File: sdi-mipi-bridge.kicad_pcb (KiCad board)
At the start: 6 copper layers, 70 x 42 mm, 203 parts, among them J1 112740-13, J2 112740-13, J3 WE_68715014522_ONE-SIDE, J4 GRPB052VWVN-RC, J5 GRPB041VWVN-RC, J6 GRPB052VWVN-RC, SW1 SW_DIP_x06, SW2 SW_DIP_x06, U1 MAX8902B, U2 GS2971A, U3 GS2988, U4 CrossLink_LIF-MD6000-6JMG80I, U5 SC18IS602BIPW, Y1 ABM7_27.000MH_D2Y_T

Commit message: Change RST pullup from 2k2 to 4k7 and note I2C pull-ups as DNP
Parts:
- R84: value R_2k2_0402 -> R_4k7_0402

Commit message: Bump release to 1.3.0
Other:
- board text added: "Rev.1.3.0 02/2021"
- board text removed: "Rev.1.2.0 12/2020"
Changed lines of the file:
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@@
-(kicad_pcb (version 20171130) (host pcbnew "(5.1.8-0-10_14)")
+(kicad_pcb (version 20171130) (host pcbnew 5.1.5+dfsg1-2~bpo10+1)
   (general
     (thickness 1.6)
@@
     (37 F.SilkS user)
     (38 B.Mask user)
-    (39 F.Mask user hide)
+    (39 F.Mask user)
     (40 Dwgs.User user hide)
     (41 Cmts.User user hide)
@@
   (gr_line (start 154.14 124.39) (end 152 122.25) (layer B.SilkS) (width 0.1))
   (gr_line (start 156.08 124.39) (end 154.14 124.39) (layer B.SilkS) (width 0.1))
-  (gr_text "Rev.1.2.0 12/2020" (at 145.5234 103.6068) (layer F.Mask)
+  (gr_text "Rev.1.3.0 02/2021" (at 145.5234 103.6068) (layer F.Mask)
     (effects (font (size 0.7 0.7) (thickness 0.15)))
   )
@@
     (effects (font (size 1 1) (thickness 0.2)))
   )
-  (gr_text "Rev.1.2.0 12/2020" (at 145.5234 103.6068) (layer F.Cu)
+  (gr_text "Rev.1.3.0 02/2021" (at 145.5234 103.6068) (layer F.Cu)
     (effects (font (size 0.7 0.7) (thickness 0.15)))
   )

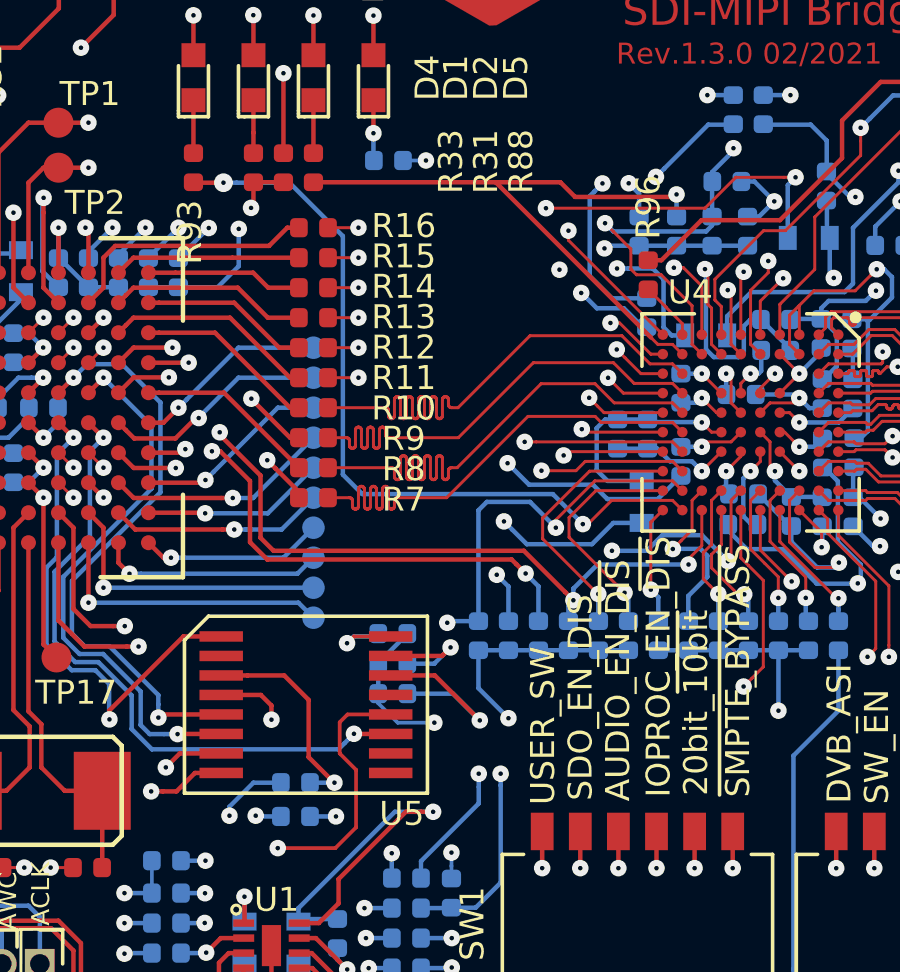
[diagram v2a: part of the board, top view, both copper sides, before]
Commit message: Update layout DRC-clean
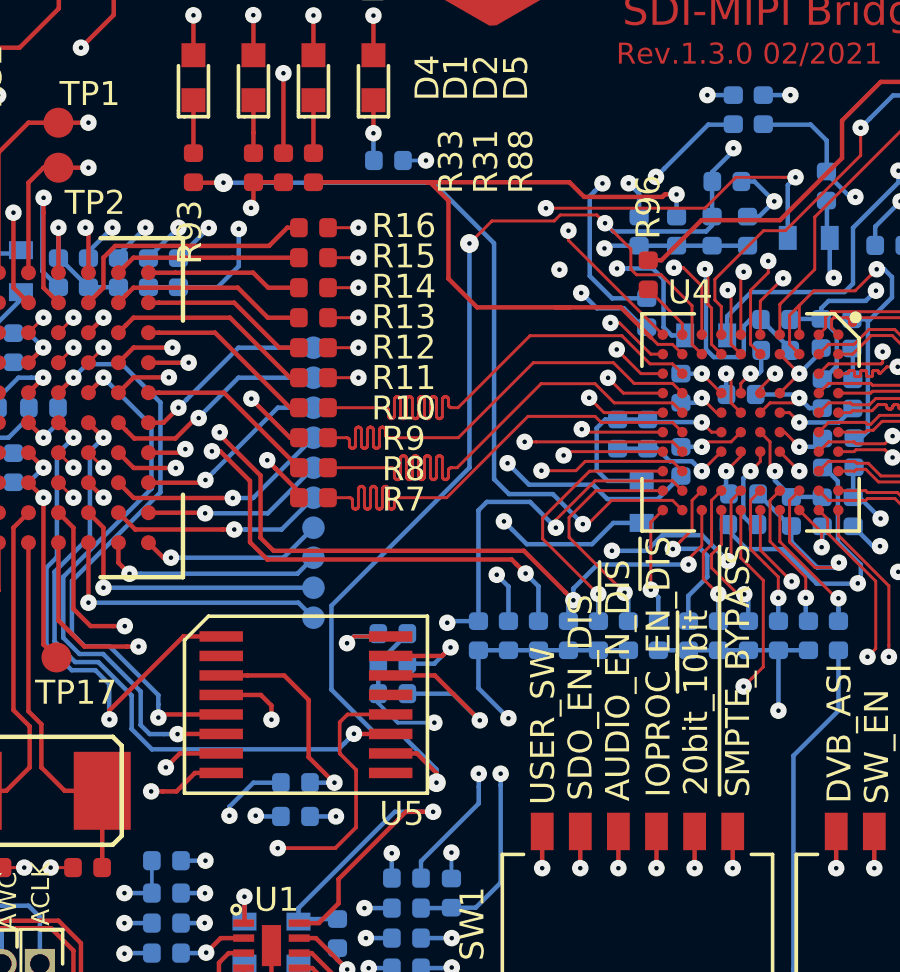
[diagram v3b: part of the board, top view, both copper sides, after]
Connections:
- R37 pad 2: /SDA_CL -> /SPI_SCK(SDA)
- R38 pad 2: /SCL_CL -> /SPI_SS(SCL)
- R41 pad 2: /SDA_CL -> /SPI_SCK(SDA)
- R42 pad 2: /SCL_CL -> /SPI_SS(SCL)
- R85 pad 2: /SCL_CL -> /SPI_SS(SCL)
- R86 pad 2: /SDA_CL -> /SPI_SCK(SDA)
- U5 pad 10: Net-(U5-Pad10) -> /CRESET_B
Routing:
- net /CRESET_B: track 29.0 -> 59.5 mm, vias 2 -> 4
- net /SPI_SCK(SDA): track 24.6 -> 43.0 mm, vias 1 -> 3
- net /SDA_CL: track 12.4 -> 0.00 mm, vias 2 -> 0
- net /SPI_SS(SCL): track 35.2 -> 45.3 mm, vias 3 -> 5
- net /SCL_CL: track 9.77 -> 0.00 mm, vias 2 -> 0
- net /CDONE: track 21.7 -> 26.0 mm
- net /MISO: track 35.8 -> 37.9 mm
- net /USER_SCL: track 23.3 -> 24.4 mm

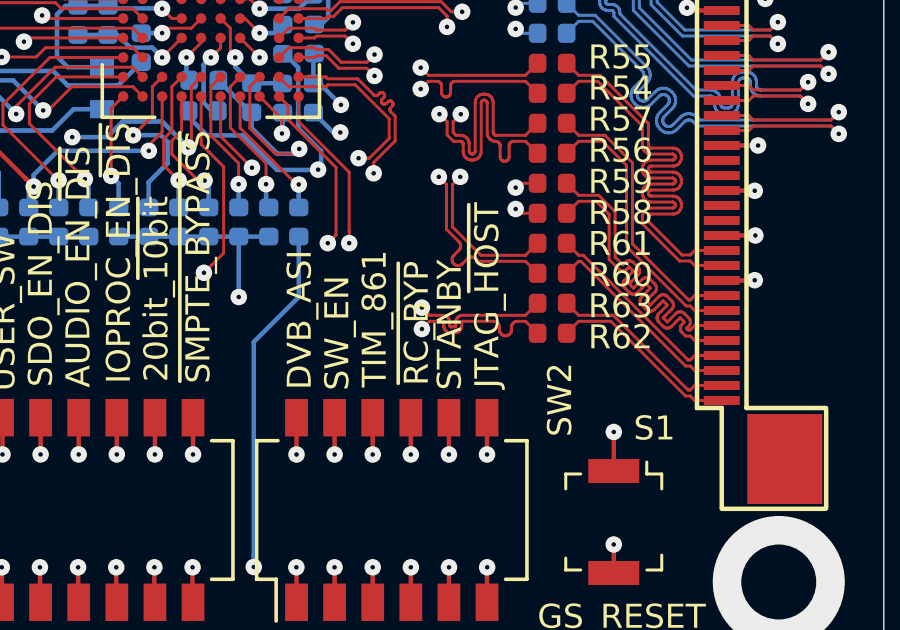
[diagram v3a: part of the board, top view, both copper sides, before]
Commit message: Update STANDBY label near SW2
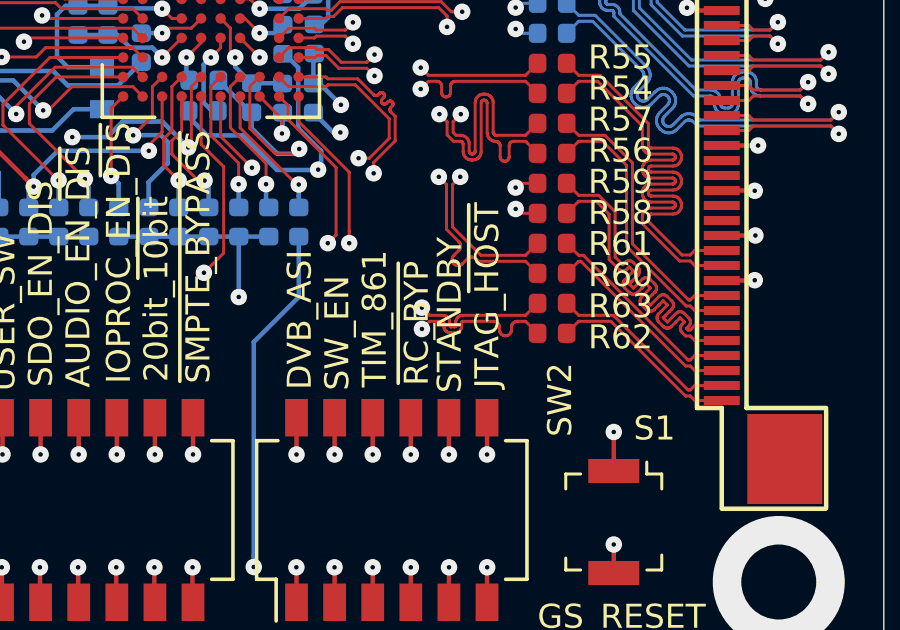
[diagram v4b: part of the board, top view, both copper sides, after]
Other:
- board text added: "STANDBY"
- board text removed: "STANBY"
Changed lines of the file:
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@@
     (35 F.Paste user hide)
     (36 B.SilkS user hide)
-    (37 F.SilkS user hide)
+    (37 F.SilkS user)
     (38 B.Mask user hide)
     (39 F.Mask user hide)
@@
     (effects (font (size 0.8 0.8) (thickness 0.12)))
   )
-  (gr_text STANBY (at 153.529 126.432429 90) (layer F.SilkS)
+  (gr_text STANDBY (at 153.529 126.1 90) (layer F.SilkS)
     (effects (font (size 0.8 0.8) (thickness 0.12)))
   )

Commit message: Ported to KiCAD 6
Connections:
- net /20bit_~10bit~ renamed /20bit_~{10bit}
- net /Audio_EN_~DIS~ renamed /Audio_EN_~{DIS}
- net /IOPROC_EN_~DIS~ renamed /IOPROC_EN_~{DIS}
- net /JTAG_~HOST~ renamed /JTAG_~{HOST}
- net /~CS~_TMS renamed /~{CS}_TMS
- net /~RC_BYP~ renamed /~{RC_BYP}
- net /~SMPTE_BYPASS~ renamed /~{SMPTE_BYPASS}
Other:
- net class Default removed
- net class Inner_Layer removed
- board text added: "20bit_~{10bit}"
- board text added: "AUDIO_EN_~{DIS}"
- board text added: "IOPROC_EN_~{DIS}"
- board text added: "JTAG_~{HOST}"
- board text added: "~{RC_BYP}"
- board text added: "~{SMPTE_BYPASS}"
- board text removed: "20bit_~10bit~"
- board text removed: "AUDIO_EN_~DIS~"
- board text removed: "IOPROC_EN_~DIS~"
- board text removed: "JTAG_~HOST~"
- board text removed: "~RC_BYP~"
- board text removed: "~SMPTE_BYPASS~"
